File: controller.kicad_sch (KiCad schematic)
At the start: 59 parts, among them J12 Conn_01x24_Pin, J13 Conn_01x24_Socket, J4 USB_C_Receptacle_USB2.0_16P, J9 Conn_01x04_Pin, SW1 SW_RST, SW2 SW_BOOT, T13 5V, T21 SCL, T24 SDA, T33 3V3, T34 GND, U1 ESP32-S3-WROOM-1_N8R2, U15 TPS2116DRL, U17 SSD1306, U2 TLV62569DBV, U6 MAX811SEUS-T, U9 24LC256

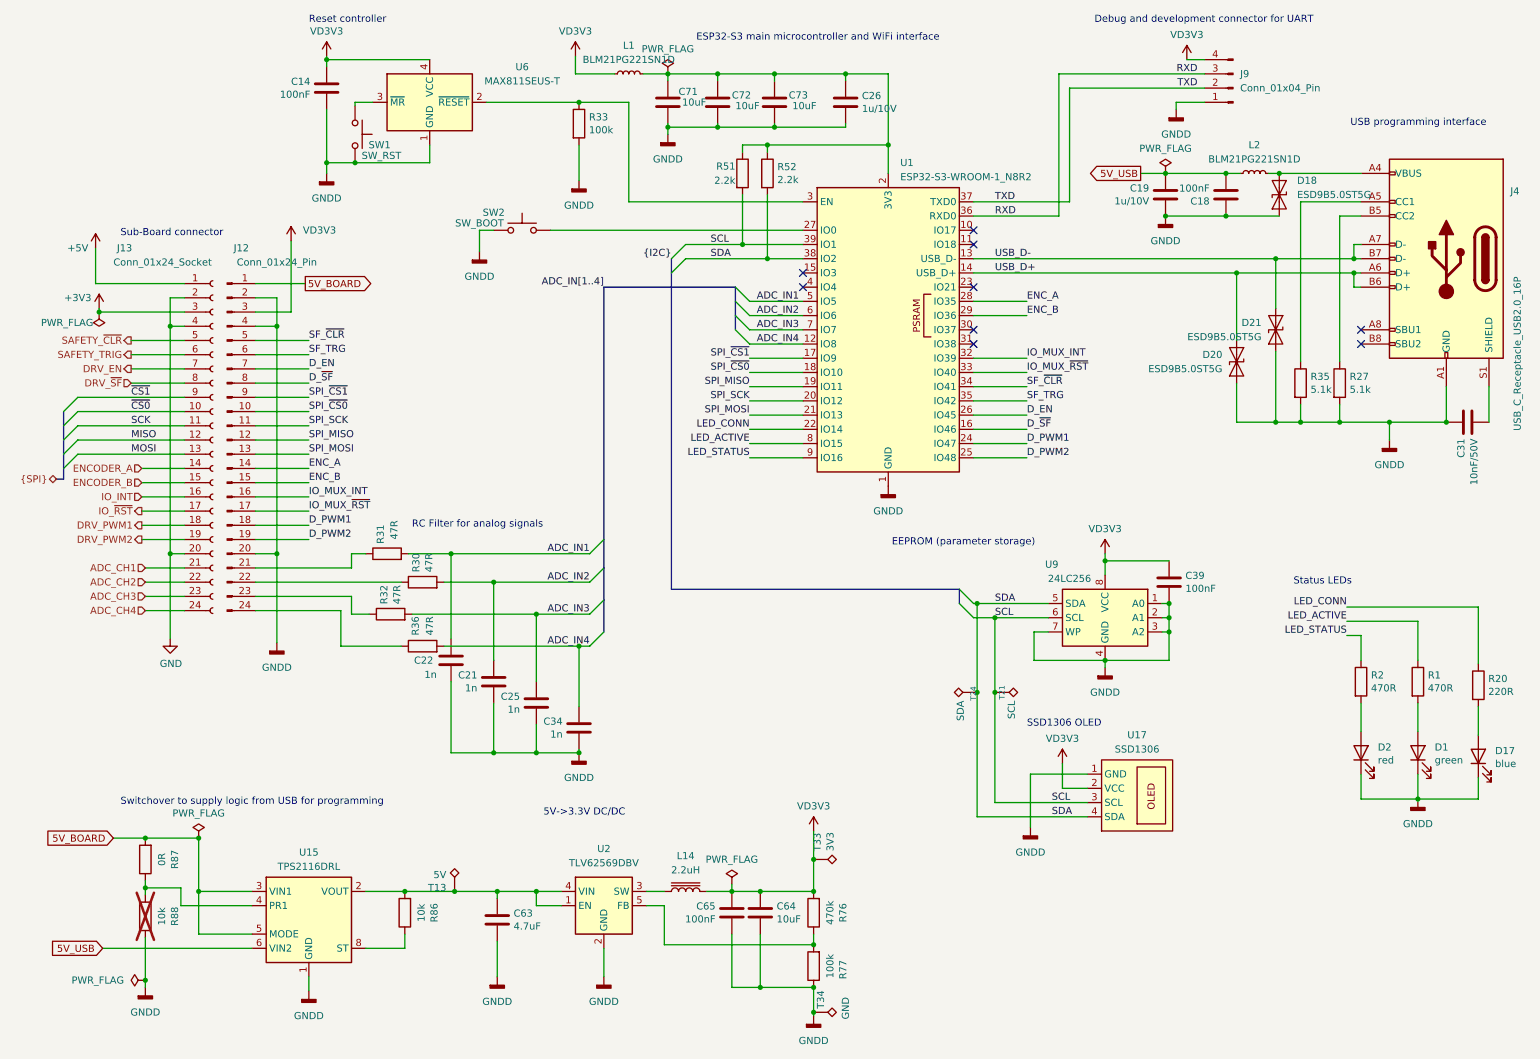
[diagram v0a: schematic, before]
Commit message: Simplified design (Old version switched to hodor-max)
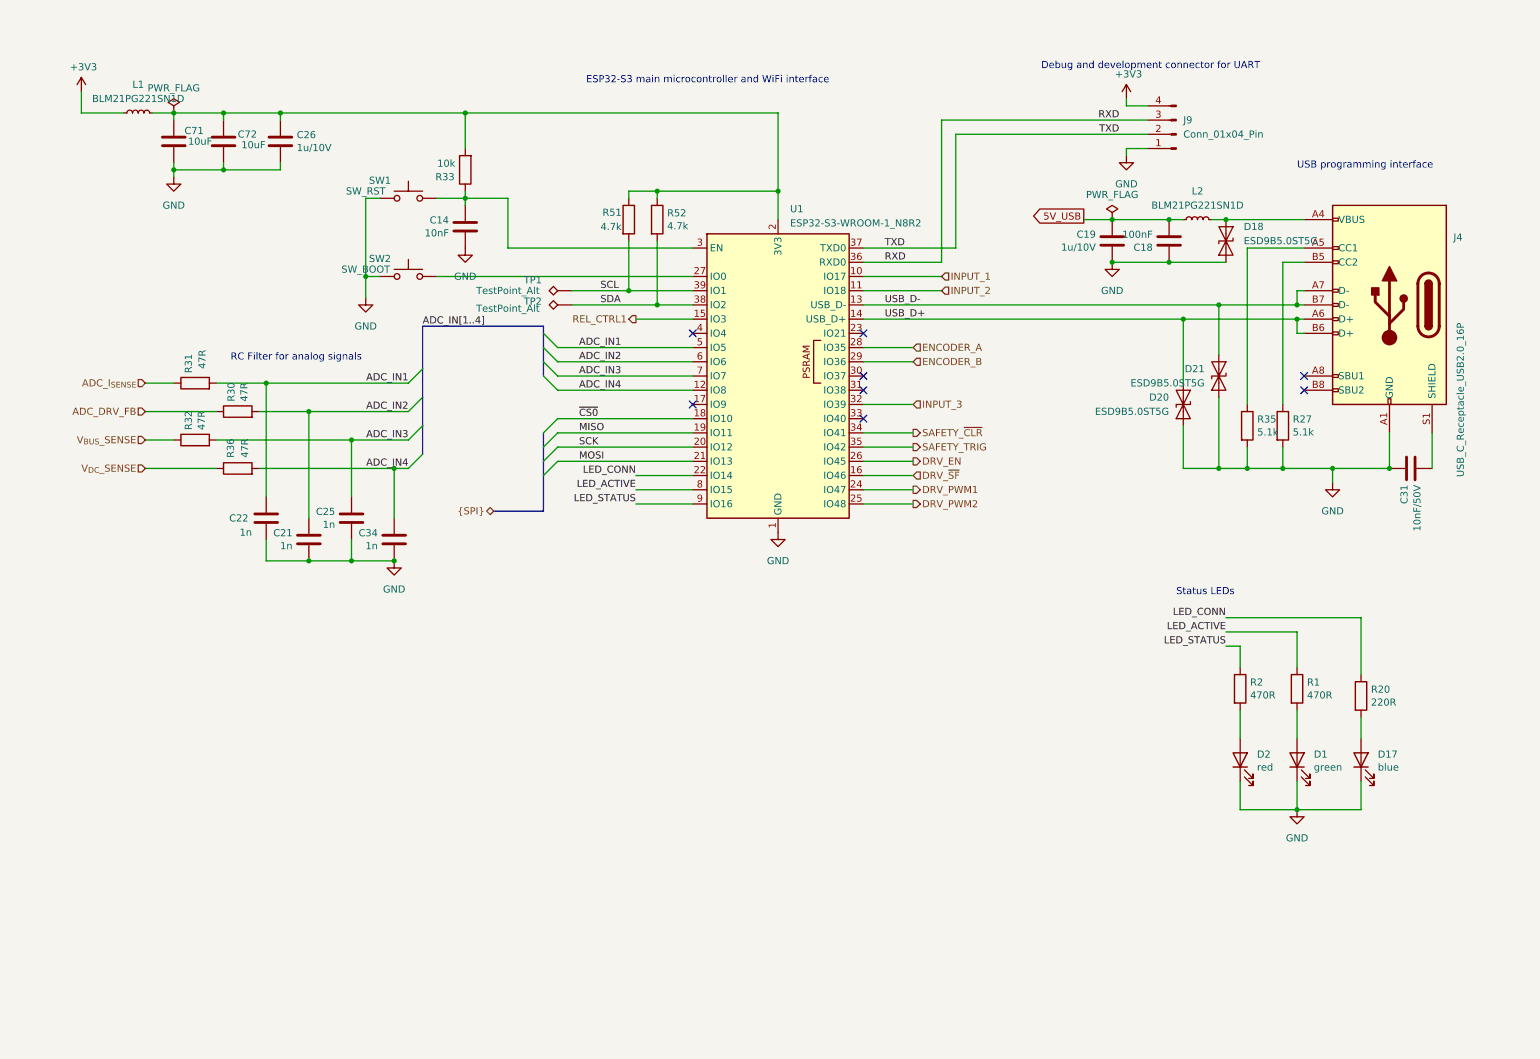
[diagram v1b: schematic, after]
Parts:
- removed C39, C65: 100nF, Capacitor_SMD:C_0402_1005Metric, symbol Device:C
- removed C63: 4.7uF, Capacitor_SMD:C_1206_3216Metric, symbol Device:C
- removed C64, C73: 10uF, Capacitor_SMD:C_0805_2012Metric, symbol Device:C
- removed J12: Conn_01x24_Pin, Connector_PinHeader_2.00mm:PinHeader_2x12_P2.00mm_Horizontal, symbol Connector:Conn_01x24_Pin
- removed J13: Conn_01x24_Socket, Connector_PinSocket_2.00mm:PinSocket_2x12_P2.00mm_Vertical, symbol Connector:Conn_01x24_Socket
- removed L14: 2.2uH, Inductor_SMD:L_1812_4532Metric, symbol Device:L_Iron
- removed R76: 470k, Resistor_SMD:R_0402_1005Metric, symbol Device:R
- removed R77: 100k, Resistor_SMD:R_0402_1005Metric, symbol Device:R
- removed R86, R88: 10k, Resistor_SMD:R_0402_1005Metric, symbol Device:R
- removed R87: 0R, Resistor_SMD:R_0402_1005Metric, symbol Device:R
- removed T13: 5V, TestPoint:TestPoint_Pad_D1.0mm, symbol Connector:TestPoint_Alt
- removed T21: SCL, TestPoint:TestPoint_Pad_D1.0mm, symbol Connector:TestPoint_Alt
- removed T24: SDA, TestPoint:TestPoint_Pad_D1.0mm, symbol Connector:TestPoint_Alt
- removed T33: 3V3, TestPoint:TestPoint_Pad_D1.0mm, symbol Connector:TestPoint_Alt
- removed T34: GND, TestPoint:TestPoint_Pad_1.0x1.0mm, symbol Connector:TestPoint_Alt
- removed U15: TPS2116DRL, Package_TO_SOT_SMD:SOT-583-8, symbol Power_Management:TPS2116DRL
- removed U17: SSD1306, hodor_footprints:SSD1306_OLED_Horizontal_Reverse, symbol hodor_custom_parts:SSD1306_OLED
- removed U2: TLV62569DBV, Package_TO_SOT_SMD:SOT-23-5, symbol Regulator_Switching:TLV62569DBV
- removed U6: MAX811SEUS-T, Package_TO_SOT_SMD:SOT-143, symbol Power_Supervisor:MAX811SEUS-T
- removed U9: 24LC256, Package_SO:TSSOP-8_4.4x3mm_P0.65mm, symbol Memory_EEPROM:24LC256
- added TP1, TP2: TestPoint_Alt, TestPoint:TestPoint_Pad_1.0x1.0mm, symbol Connector:TestPoint_Alt
- C14: value 100nF -> 10nF
- D1, D17, D2: footprint LED_SMD:LED_Kingbright_APA1606_1.6x0.6mm_Horizontal -> LED_SMD:LED_0603_1608Metric
- J9: footprint hodor_footprints:Conn_Header2.54_1x04_SMD -> Connector_PinHeader_2.54mm:PinHeader_1x04_P2.54mm_Vertical
- R33: value 100k -> 10k
- R51, R52: value 2.2k -> 4.7k
- SW1, SW2: footprint Button_Switch_SMD:SW_SPST_CK_KMS2xxG -> Button_Switch_SMD:SW_Push_SPST_NO_Alps_SKRK
- U1: footprint RF_Module:ESP32-S3-WROOM-1 -> RF_Module:ESP32-S3-WROOM-1U
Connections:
- net D_EN is gone; now on net DRV_EN: U1.26 (IO45)
- net D_PWM1 is gone; now on net DRV_PWM1: U1.24 (IO47)
- net D_PWM2 is gone; now on net DRV_PWM2: U1.25 (IO48)
- net D_~{SF} is gone; now on net DRV_~{SF}: U1.16 (IO46)
- net ENC_A is gone; now on net ENCODER_A: U1.28 (IO35)
- net ENC_B is gone; now on net ENCODER_B: U1.29 (IO36)
- net SF_TRG is gone; now on net SAFETY_TRIG: U1.35 (IO42)
- net SF_~{CLR} is gone; now on net SAFETY_~{CLR}: U1.34 (IO41)
- net SPI_MISO is gone; now on net MISO: U1.19 (IO11)
- net SPI_MOSI is gone; now on net MOSI: U1.21 (IO13)
- net SPI_SCK is gone; now on net SCK: U1.20 (IO12)
- net SPI_~{CS0} is gone; now on net ~{CS0}: U1.18 (IO10)
- net +3V3: now also J9.4 (Pin_4), L1.1
- net 5V_USB: no longer C18.1, C19.2, L2.1
- net GND: now also C14.1, C18.2, C19.1, C21.1, C22.1, C25.1, C26.1, C31.2, C34.1, C71.2, C72.2, D1.1 (K), D17.1 (K), D18.1 (A1), D2.1 (K), D20.1 (A1), D21.1 (A1), J4.A1 (GND), J4.A12 (GND), J4.B1 (GND), J4.B12 (GND), J9.1 (Pin_1), R27.2, R35.2, SW1.1, SW2.1, U1.1 (GND), U1.40 (GND), U1.41 (GND)
- net SCL: now also TP1.1
- net SDA: now also TP2.1
- net at C26.2, C71.1, C72.1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: now also R33.2
- net ADC_I_{SENSE}: now reaches R31.1
- net ADC_DRV_FB: now reaches R30.1
- net V_{BUS}_SENSE: now reaches R32.1
- net V_{DC}_SENSE: now reaches R36.1
- net at SW1.2: now also C14.2, R33.1, U1.3 (EN)
- net INPUT_1: now reaches U1.10 (IO17)
- net INPUT_2: now reaches U1.11 (IO18)
- net REL_CTRL1: now reaches U1.15 (IO3)
- removed net GNDD: C14.1, C18.2, C19.1, C21.1, C22.1, C25.1, C26.1, C31.2, C34.1, C71.2, C72.2, D1.1 (K), D17.1 (K), D18.1 (A1), D2.1 (K), D20.1 (A1), D21.1 (A1), J4.A1 (GND), J4.A12 (GND), J4.B1 (GND), J4.B12 (GND), J9.1 (Pin_1), R27.2, R33.2, R35.2, SW1.1, SW2.1, U1.1 (GND), U1.40 (GND), U1.41 (GND)
- net IO_MUX_INT renamed INPUT_3
- net IO_MUX_~{RST}: no longer names the net of U1.33 (IO40)
- net SPI_~{CS1}: no longer names the net of U1.17 (IO9)
- removed net VD3V3: C14.2, J9.4 (Pin_4), L1.1
- new net: C18.1, C19.2, L2.1
- no-connect marks 9 -> 8
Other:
- note removed: "5V->3.3V DC/DC"
- note removed: "EEPROM (parameter storage)"
- note removed: "Reset controller"
- note removed: "SSD1306 OLED"
- note removed: "Sub-Board connector"
- note removed: "Switchover to supply logic from USB for programming"
- moved on the sheet: C14, C18, C19, C21, C22, C25, C26, C31, C34, C71, C72, D1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

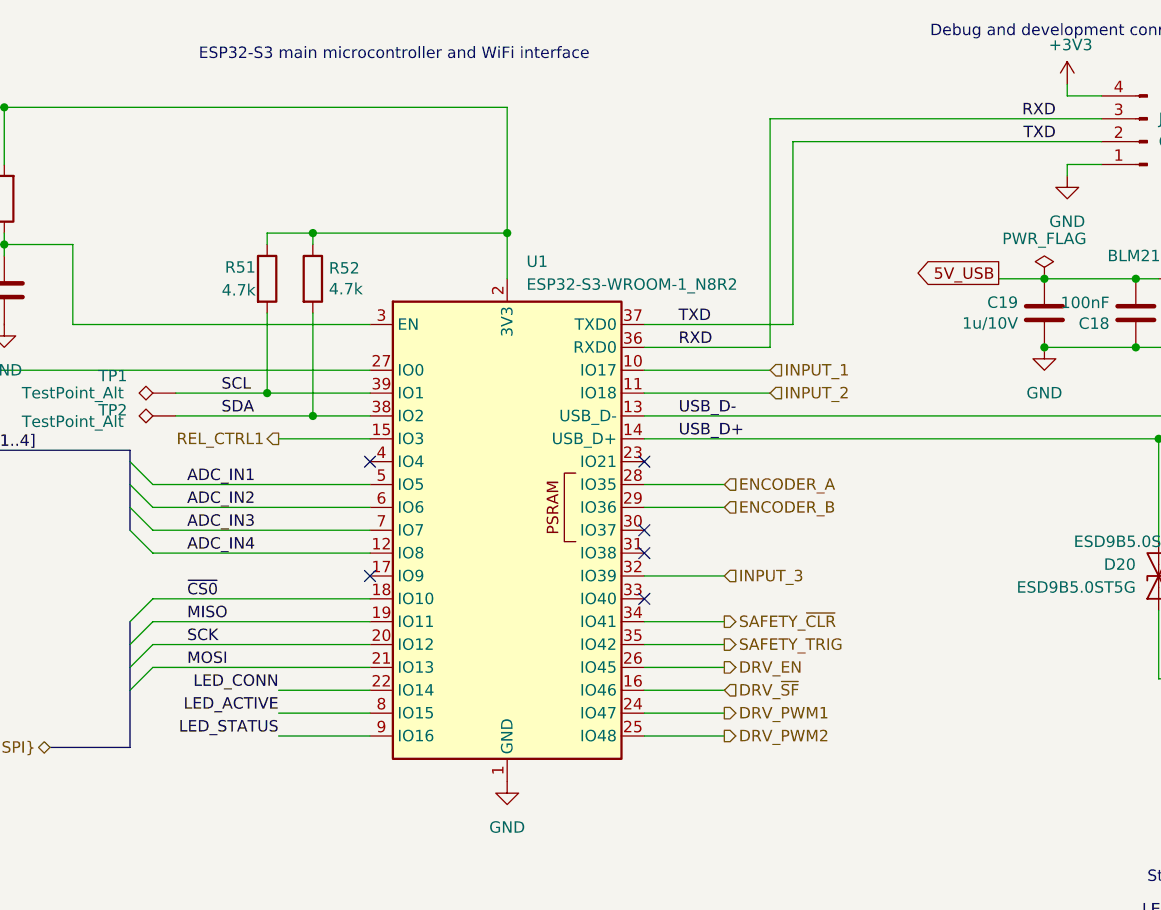
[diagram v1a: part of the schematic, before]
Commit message: All nets connected
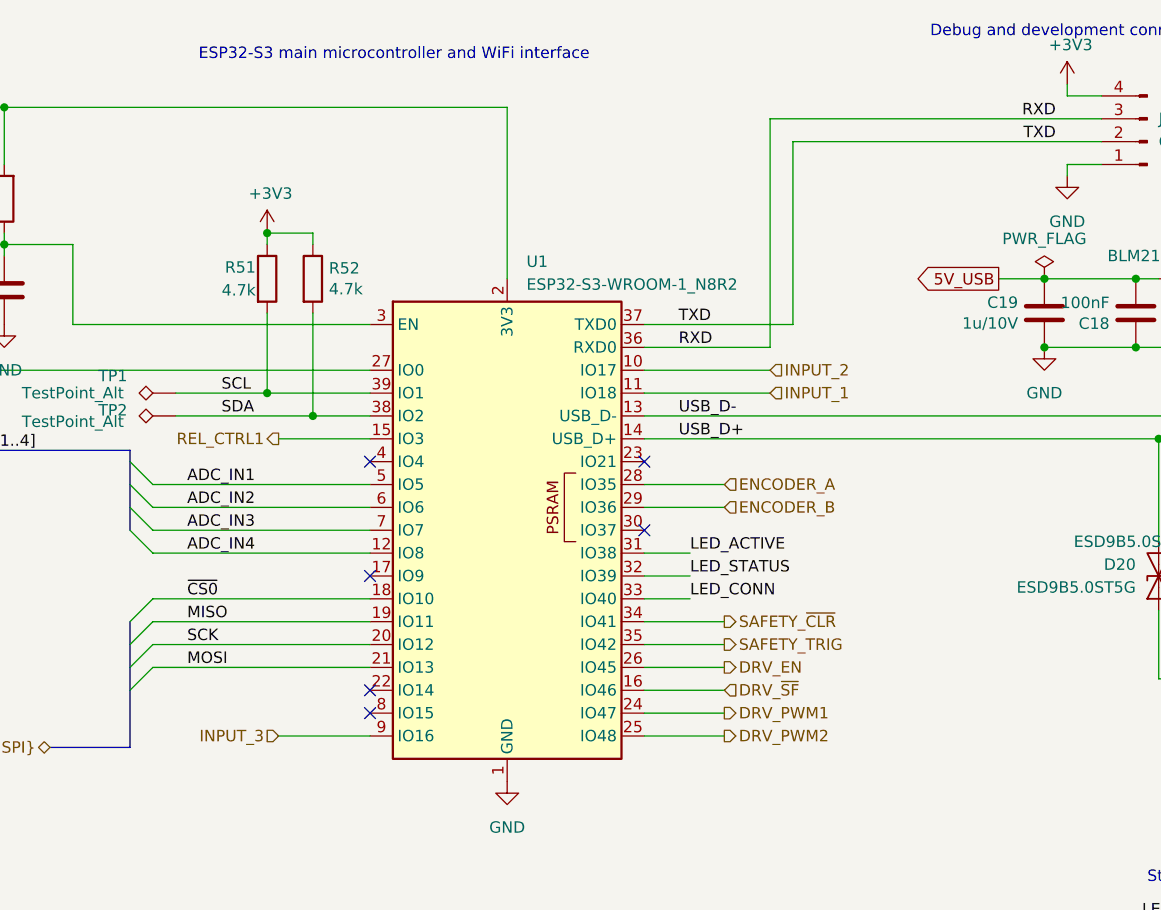
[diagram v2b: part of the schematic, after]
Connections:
- net +3V3: now also R51.1, R52.1
- net 5V_USB: now also C18.1, C19.2, L2.1
- net INPUT_1: now also U1.11 (IO18); no longer U1.10 (IO17)
- net INPUT_2: now also U1.10 (IO17); no longer U1.11 (IO18)
- net INPUT_3: now also U1.9 (IO16); no longer U1.32 (IO39)
- net LED_ACTIVE: now also U1.31 (IO38); no longer U1.8 (IO15)
- net LED_CONN: now also U1.33 (IO40); no longer U1.22 (IO14)
- net LED_STATUS: now also U1.32 (IO39); no longer U1.9 (IO16)
- net at C26.2, C71.1, C72.1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: no longer R51.1, R52.1
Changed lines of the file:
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@@
 	)
 	(junction
-		(at 128.27 45.72)
-		(diameter 0)
-		(color 0 0 0 0)
-	)
-	(junction
 		(at 93.98 46.99)
 		(diameter 0)
@@
 	)
 	(junction
+		(at 123.19 45.72)
+		(diameter 0)
+		(color 0 0 0 0)
+	)
+	(junction
 		(at 248.92 95.25)
 		(diameter 0)
@@
 	)
 	(junction
-		(at 149.86 45.72)
-		(diameter 0)
-		(color 0 0 0 0)
-	)
-	(junction
 		(at 123.19 63.5)
 		(diameter 0)
@@
 	)
 	(no_connect
-		(at 165.1 81.28)
+		(at 165.1 78.74)
 	)
 	(no_connect
-		(at 165.1 78.74)
+		(at 134.62 96.52)
 	)
 	(no_connect
@@
 	)
 	(no_connect
-		(at 165.1 86.36)
+		(at 134.62 83.82)
 	)
 	(no_connect
-		(at 134.62 83.82)
+		(at 134.62 99.06)
 	)
 	(bus_entry
@@
 	(wire
 		(pts
-			(xy 124.46 99.06) (xy 134.62 99.06)
-		)
-		(stroke
-			(width 0)
-			(type default)
-		)
-	)
-	(wire
-		(pts
 			(xy 60.96 40.64) (xy 60.96 41.91)
 		)
@@
 	(wire
 		(pts
-			(xy 149.86 45.72) (xy 149.86 50.8)
+			(xy 149.86 31.75) (xy 149.86 50.8)
 		)
 		(stroke
@@
 	(wire
 		(pts
+			(xy 165.1 86.36) (xy 170.18 86.36)
+		)
+		(stroke
+			(width 0)
+			(type default)
+		)
+	)
+	(wire
+		(pts
 			(xy 93.98 46.99) (xy 101.6 46.99)
 		)
@@
 	(wire
 		(pts
-			(xy 124.46 96.52) (xy 134.62 96.52)
-		)
-		(stroke
-			(width 0)
-			(type default)
-		)
-	)
-	(wire
-		(pts
 			(xy 41.91 41.91) (xy 50.8 41.91)
 		)
@@
 	(wire
 		(pts
-			(xy 165.1 83.82) (xy 173.99 83.82)
-		)
-		(stroke
-			(width 0)
-			(type default)
-		)
-	)
-	(wire
-		(pts
 			(xy 76.2 46.99) (xy 76.2 60.96)
 		)
@@
 	(wire
 		(pts
-			(xy 110.49 73.66) (xy 134.62 73.66)
+			(xy 165.1 81.28) (xy 170.18 81.28)
 		)
 		(stroke
@@
 	(wire
 		(pts
-			(xy 149.86 31.75) (xy 149.86 45.72)
+			(xy 110.49 73.66) (xy 134.62 73.66)
 		)
 		(stroke
@@
 	(wire
 		(pts
+			(xy 165.1 83.82) (xy 170.18 83.82)
+		)
+		(stroke
+			(width 0)
+			(type default)
+		)
+	)
+	(wire
+		(pts
 			(xy 222.25 68.58) (xy 222.25 80.01)
 		)
@@
 	(wire
 		(pts
-			(xy 128.27 45.72) (xy 149.86 45.72)
-		)
-		(stroke
-			(width 0)
-			(type default)
-		)
-	)
-	(wire
-		(pts
 			(xy 173.99 101.6) (xy 165.1 101.6)
 		)
@@
 		)
 	)
+	(label "LED_ACTIVE"
+		(at 170.18 81.28 0)
+		(effects
+			(font
+				(size 1.27 1.27)
+			)
+			(justify left bottom)
+		)
+	)
 	(label "MOSI"
 		(at 114.3 93.98 0)
@@
 		)
 	)
-	(label "ADC_IN1"
-		(at 114.3 73.66 0)
+	(label "LED_CONN"
+		(at 170.18 86.36 0)
 		(effects
 			(font
@@
 		)
 	)
-	(label "TXD"
-		(at 168.91 55.88 0)
+	(label "ADC_IN1"
+		(at 114.3 73.66 0)
 		(effects
 			(font
@@
 		)
 	)
-	(label "LED_ACTIVE"
-		(at 124.46 99.06 180)
+	(label "TXD"
+		(at 168.91 55.88 0)
 		(effects
 			(font
 				(size 1.27 1.27)
 			)
-			(justify right bottom)
+			(justify left bottom)
 		)
 	)
@@
 		)
 	)
+	(label "LED_STATUS"
+		(at 170.18 83.82 0)
+		(effects
+			(font
+				(size 1.27 1.27)
+			)
+			(justify left bottom)
+		)
+	)
 	(label "ADC_IN3"
 		(at 114.3 78.74 0)
@@
 		)
 	)
-	(label "LED_STATUS"
-		(at 124.46 101.6 180)
-		(effects
-			(font
-				(size 1.27 1.27)
-			)
-			(justify right bottom)
-		)
-	)
 	(label "ADC_IN4"
 		(at 114.3 81.28 0)
@@
 		)
 	)
-	(label "LED_CONN"
-		(at 124.46 96.52 180)
-		(effects
-			(font
-				(size 1.27 1.27)
-			)
-			(justify right bottom)
-		)
-	)
 	(label "USB_D+"
 		(at 168.91 68.58 0)
@@
 	(global_label "5V_USB"
 		(shape output)
-		(at 204.47 50.165 180)
+		(at 204.47 50.8 180)
 		(fields_autoplaced yes)
 		(effects
@@
 		)
 		(property "Intersheetrefs" "${INTERSHEET_REFS}"
-			(at 194.4091 50.165 0)
+			(at 194.4091 50.8 0)
 			(effects
 				(font
@@
 	(hierarchical_label "INPUT_3"
 		(shape input)
-		(at 173.99 83.82 0)
+		(at 124.46 101.6 180)
 		(effects
 			(font
 				(size 1.27 1.27)
 			)
-			(justify left)
+			(justify right)
 		)
 	)
@@
 		)
 	)
-	(hierarchical_label "{SPI}"
-		(shape bidirectional)
-		(at 99.06 102.87 180)
+	(hierarchical_label "INPUT_2"
+		(shape input)
+		(at 179.07 60.96 0)
 		(effects
 			(font
 				(size 1.27 1.27)
 			)
-			(justify right)
+			(justify left)
 		)
 	)
-	(hierarchical_label "INPUT_2"
-		(shape input)
-		(at 179.07 63.5 0)
+	(hierarchical_label "{SPI}"
+		(shape bidirectional)
+		(at 99.06 102.87 180)
 		(effects
 			(font
 				(size 1.27 1.27)
 			)
-			(justify left)
+			(justify right)
 		)
 	)
@@
 		)
 	)
-	(hierarchical_label "INPUT_1"
+	(hierarchical_label "ENCODER_A"
 		(shape input)
-		(at 179.07 60.96 0)
+		(at 173.99 73.66 0)
 		(effects
 			(font
@@
 		)
 	)
-	(hierarchical_label "ENCODER_A"
+	(hierarchical_label "INPUT_1"
 		(shape input)
-		(at 173.99 73.66 0)
+		(at 179.07 63.5 0)
 		(effects
 			(font
@@
 					(unit 1)
 				)
+			)
+		)
+	)
+	(symbol
+		(lib_id "power:+3V3")
+		(at 123.19 45.72 0)
+		(unit 1)
+		(exclude_from_sim no)
+		(in_bom yes)
+		(on_board yes)
+		(dnp no)
+		(property "Reference" "#PWR05"
+			(at 123.19 49.53 0)
+			(effects
+				(font
+					(size 1.27 1.27)
+				)
+				(hide yes)
+			)
+		)
+		(property "Value" "+3V3"
+			(at 123.571 41.3258 0)
+			(effects
+				(font
+					(size 1.27 1.27)
+				)
+			)
+		)
+		(property "Footprint" ""
+			(at 123.19 45.72 0)
+			(effects
+				(font
+					(size 1.27 1.27)
+				)
+				(hide yes)
+			)
+		)
+		(property "Datasheet" ""
+			(at 123.19 45.72 0)
+			(effects
+				(font
+					(size 1.27 1.27)
+				)
+				(hide yes)
+			)
+		)
+		(property "Description" "Power symbol creates a global label with name \"+3V3\""
+			(at 123.19 45.72 0)
+			(effects
+				(font
+					(size 1.27 1.27)
+				)
+				(hide yes)
+			)
+		)
+		(pin "1"
+		)
+		(instances
+			(project "hodor_hardware"
+				(path "/2da01e60-41ef-423d-82f4-a5c8908d8b96/efd4ec69-52b7-4b82-b6f7-297e43729fd0"
+					(reference "#PWR05")
+					(unit 1)
+				)

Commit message: Finalized Layout
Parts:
- C19: renamed from C31; value 10nF/50V -> 10nF/25V
- R39: renamed from R51; value 4.7k -> 5.1k
- R40: renamed from R52; value 4.7k -> 5.1k
- renumbered C19 to C23, C18 to C24, C25 to C30, C21 to C31, C22 to C32, C34 to C33, C72 to C34, C14 to C35, C71 to C36, C26 to C37, D18 to D10, D20 to D12, D21 to D13, D1 to D18, D2 to D19, D17 to D20, J9 to J5, L2 to L6, L1 to L8, R27 to R15, R35 to R18, R32 to R21, R31 to R22, R36 to R26, R30 to R27, R33 to R28, R1 to R41, R2 to R42, R20 to R43, U1 to U9
